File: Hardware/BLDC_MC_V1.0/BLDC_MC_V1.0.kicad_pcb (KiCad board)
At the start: 8 copper layers, 120 x 55 mm, 227 parts, among them J3 USB_C_Receptacle_USB2.0_16P, J4 Conn_02x03_Counter_Clockwise, J5 S6B-PH-K-S_LF__SN_, J6 XT60-M, J7 1714984, J8 S10B-PHDSS LFSN, Q1 BSC027N10NS5ATMA1, Q2 BSC027N10NS5ATMA1, Q3 BSC027N10NS5ATMA1, Q4 BSC027N10NS5ATMA1, Q5 BSC027N10NS5ATMA1, Q6 BSC027N10NS5ATMA1, Q7 BSC027N10NS5ATMA1, SW1 SW_Push, U1 LM76005RNPR, U10 TLV9061IDBVR, U11 TLV9061IDBVR, U12 TLV9061IDBVR, U13 TLV9061IDBVR, U14 TLV9061IDBVR, U15 TLV9061IDBVR, U16 LM74700QDRQ1, U2 TCAN334DR, U3 TLV9061IDBVR, U4 STM32G431RBT6, U5 LDL1117S33R, U6 DRV8353HRTAR, U7 NCV4274ADT50RKG, U8 25LC256-E_SN, U9 USBLC6-2SC6, Y1 7M-24.000MAAJ-T, Y2 ABS07-32.768KHZ-T

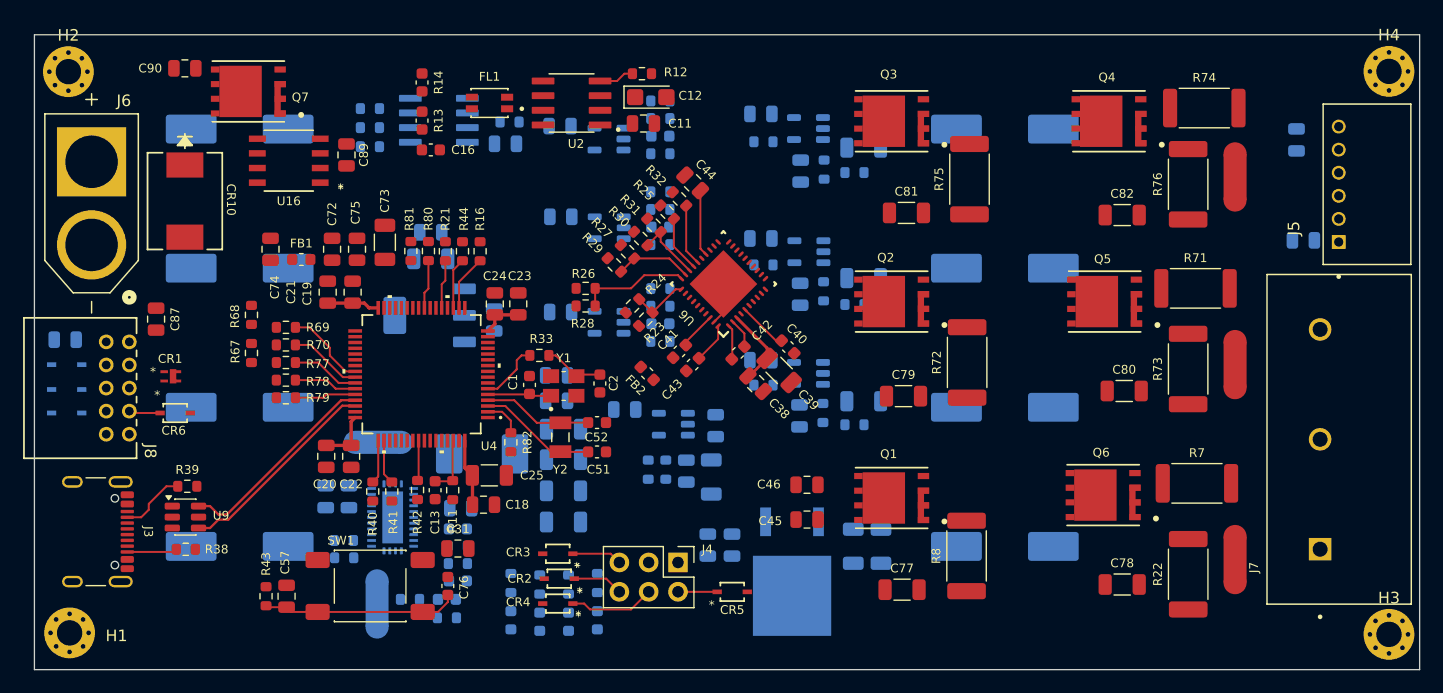
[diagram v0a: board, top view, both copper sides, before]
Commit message: Routing Power plans and change the power connedtors
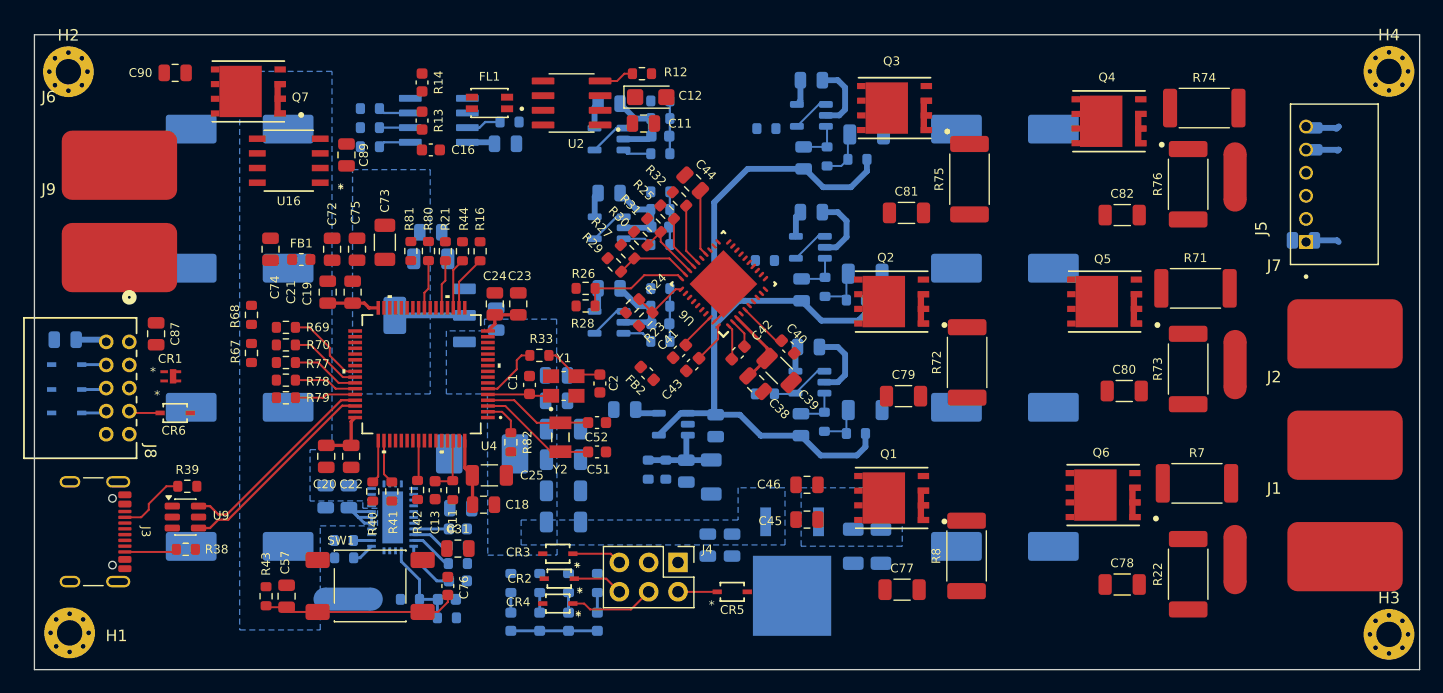
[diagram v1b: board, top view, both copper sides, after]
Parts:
- removed NT5: NetTie_2, NetTie:NetTie-2_SMD_Pad2.0mm
- added J1: Conn_01x01_Pin, BLDC_Motor_Driver_Components_Footprint:PWR_CON_L, F.Cu at (151.0, 58.8)
- added J2: Conn_01x01_Pin, BLDC_Motor_Driver_Components_Footprint:PWR_CON_L, F.Cu at (151.0, 49.1)
- added J9: Conn_01x01_Pin, BLDC_Motor_Driver_Components_Footprint:PWR_CON_L, F.Cu at (44.8, 32.9)
- CR10: moved to B.Cu
- J6: value XT60-M -> Conn_01x01_Pin; footprint BLDC_Motor_Driver_Components_Footprint:AMASS_XT60-M -> BLDC_Motor_Driver_Components_Footprint:PWR_CON_L
- J7: value 1714984 -> Conn_01x01_Pin; footprint BLDC_Motor_Driver_Components_Footprint:PHOENIX_1714984 -> BLDC_Motor_Driver_Components_Footprint:PWR_CON_L
- moved J7 24.1 mm to (151.0, 39.5), turned to 0 degrees
- moved CR10 7.33 mm to (43.2, 28.4)
- moved C85 5.26 mm to (104.8, 17.5), turned to 0 degrees
- moved C84 4.93 mm to (104.8, 29.0), turned to 0 degrees
- moved C17 4.67 mm to (87.2, 19.6), turned to 0 degrees
- moved C63 4.67 mm to (87.2, 35.6), turned to 0 degrees
- moved C62 4.66 mm to (87.2, 27.3), turned to 0 degrees
- moved C83 4.27 mm to (104.5, 40.6), turned to 0 degrees
- moved J6 4.09 mm to (44.8, 24.9), turned to 0 degrees
- moved J5 2.83 mm to (150.1, 26.5)
- moved NT4 2.54 mm to (64.6, 62.5), turned to 0 degrees
- moved C64 1.54 mm to (148.3, 22.6)
- moved C87 1.27 mm to (48.0, 39.5)
- moved Q3 1.17 mm to (112.0, 19.9)
- moved R62 1.17 mm to (108.8, 24.4)
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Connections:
- net /BLDC_MC_V1.0_CAN_Transceiver/SHDN renamed /BLDC_MC_V1.0_CAN_Transceiver/CAN_SHDN
- net /BLDC_MC_V1.0_CAN_Transceiver/STB renamed /BLDC_MC_V1.0_CAN_Transceiver/CAN_STB
- C31 pad 2: GND -> AGND
- C33 pad 2: GND -> AGND
- C34 pad 2: GND -> AGND
- C45 pad 2: PGND -> GND
- C46 pad 2: PGND -> GND
- C47 pad 2: PGND -> GND
- C48 pad 2: PGND -> GND
- C49 pad 2: PGND -> GND
- C50 pad 2: PGND -> GND
- FB2 pad 1: PGND -> GND
- J7 pad 1: /BLDC_MC_V1.0_3Phase_Inverter_legs/Phase_A -> /BLDC_MC_V1.0_3Phase_Inverter_legs/Phase_C
- NT1 pad 1: PGND -> GND
- NT2 pad 1: PGND -> GND
- NT3 pad 1: PGND -> GND
- R1 pad 2: GND -> AGND
- R3 pad 2: GND -> AGND
- R4 pad 2: GND -> AGND
- U1 pad 19: GND -> AGND
- U1 pad 24: PGND -> GND
- U1 pad 25: PGND -> GND
- U1 pad 26: PGND -> GND
- U1 pad 27: GND -> AGND
- U1 pad 28: GND -> AGND
- U1 pad 29: GND -> AGND
- U1 pad 30: GND -> AGND
- U6 pad 39: PGND -> GND
- U6 pad 41: PGND -> GND
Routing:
- net /BLDC_MC_V1.0_Voltage_Sensor/+1.65V: track 0.00 -> 80.5 mm
- net GND: track 0.00 -> 53.8 mm
- net +3.3V: track 24.5 -> 50.5 mm
- net Net-(U1-FB): track 0.00 -> 8.07 mm
- net Vin: track 0.00 -> 7.94 mm
- net /BLDC_MC_V1.0_Voltage_Sensor/1.65_No_Buffer: track 0.00 -> 7.68 mm
- net Net-(U13-IN-): track 0.00 -> 5.14 mm
- net Net-(U1-SS/TRK): track 0.00 -> 4.88 mm
- net +5V: track 0.00 -> 4.85 mm
- net Net-(C60-Pad1): track 0.00 -> 4.57 mm
- net Net-(C59-Pad1): track 0.00 -> 4.57 mm
- net Net-(C58-Pad1): track 0.00 -> 4.57 mm
- net Net-(R58-Pad2): track 0.00 -> 4.34 mm
- net Net-(R61-Pad2): track 0.00 -> 4.27 mm
- net Net-(R55-Pad2): track 0.00 -> 4.09 mm
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- added copper zone on B.Cu, net +12V
- added copper zone on B.Cu, net +3.3V
- added copper zone on B.Cu, net +5V
- added copper zone on In1.Cu, net GND
- added copper zone on In4.Cu, net GND
- added copper zone on In6.Cu, net GND
- added copper zone on B.Cu, net Vin
